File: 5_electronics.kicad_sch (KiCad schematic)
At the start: 10 parts, among them J1 Conn_02x20_Odd_Even

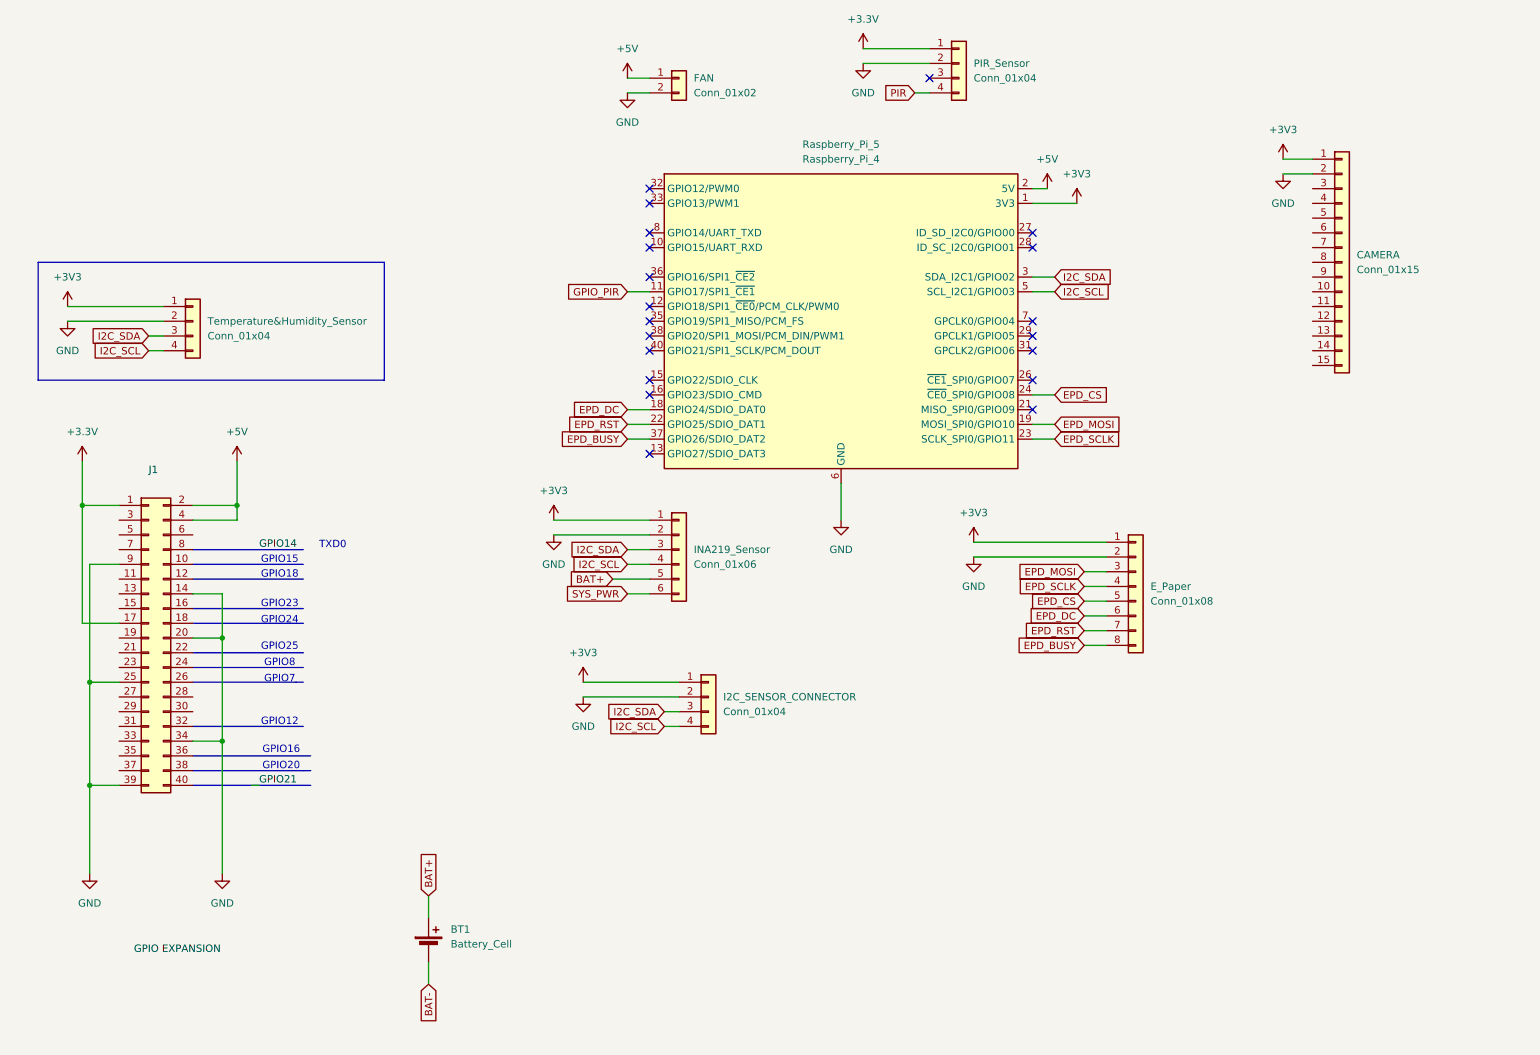
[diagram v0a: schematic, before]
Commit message: Update gpio pins
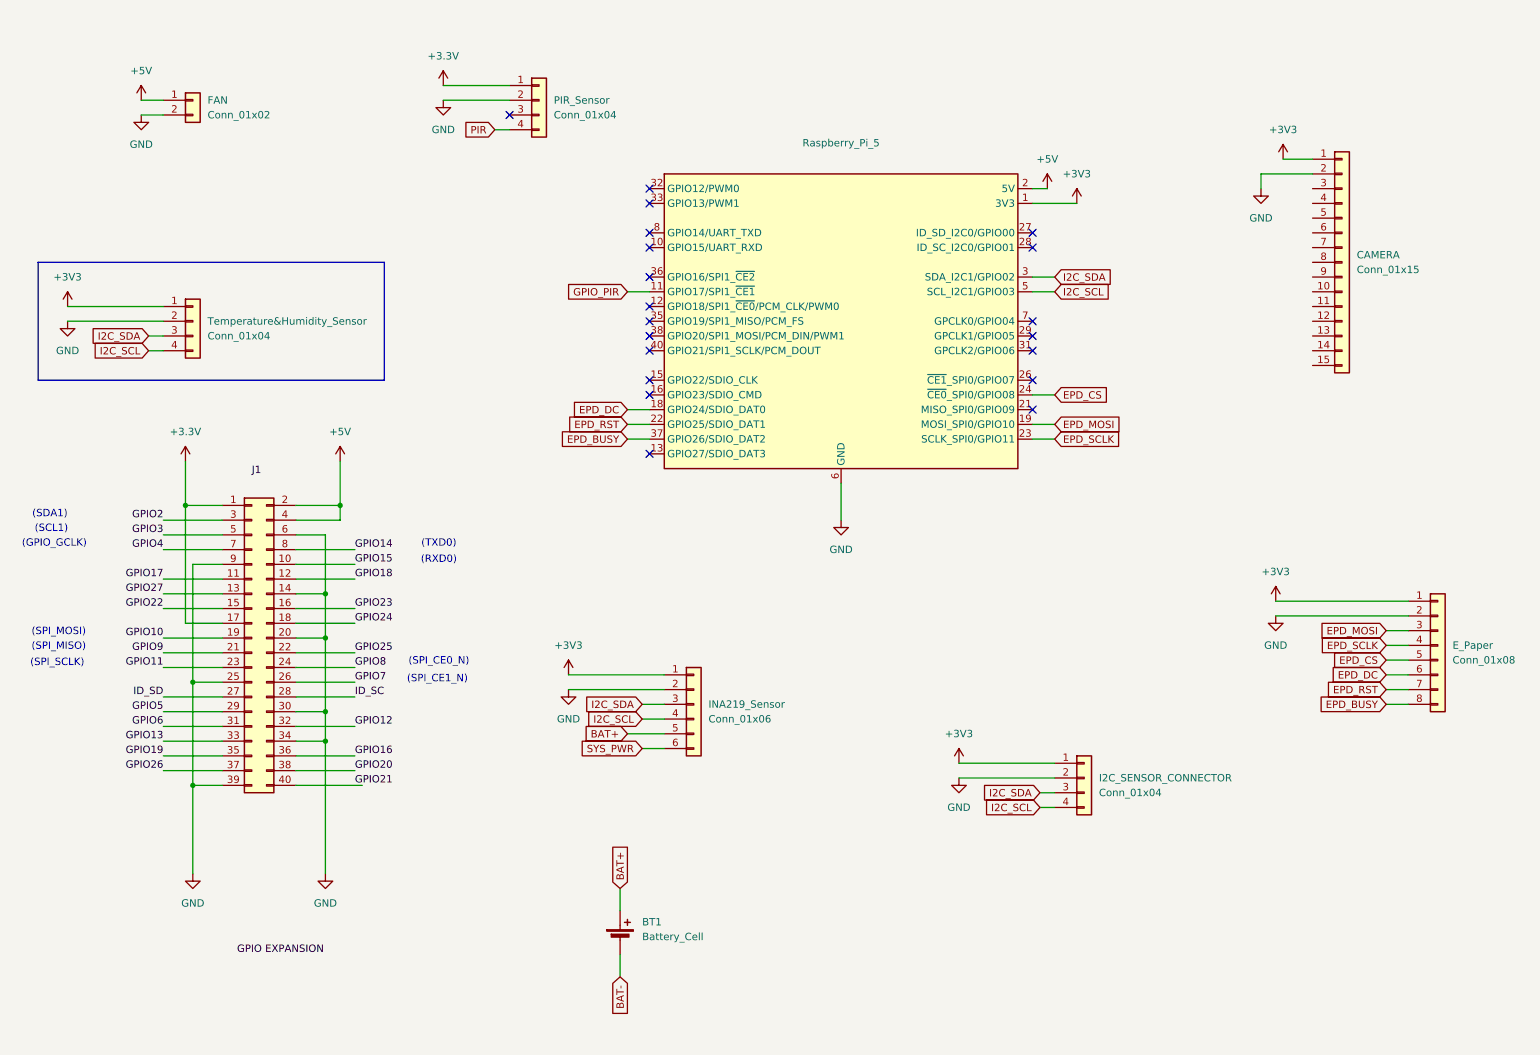
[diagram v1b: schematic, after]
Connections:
- net GND: now also J1.30 (Pin_30), J1.6 (Pin_6)
- net GPIO14: now also J1.8 (Pin_8)
- net GPIO15: now reaches J1.10 (Pin_10)
- net GPIO17: now reaches J1.11 (Pin_11)
- net GPIO18: now reaches J1.12 (Pin_12)
- net GPIO27: now reaches J1.13 (Pin_13)
- net GPIO22: now reaches J1.15 (Pin_15)
- net GPIO23: now reaches J1.16 (Pin_16)
- net GPIO24: now reaches J1.18 (Pin_18)
- net GPIO10: now reaches J1.19 (Pin_19)
- net GPIO9: now reaches J1.21 (Pin_21)
- net GPIO25: now reaches J1.22 (Pin_22)
- net GPIO11: now reaches J1.23 (Pin_23)
- net GPIO8: now reaches J1.24 (Pin_24)
- net GPIO7: now reaches J1.26 (Pin_26)
- net ID_SD: now reaches J1.27 (Pin_27)
- net ID_SC: now reaches J1.28 (Pin_28)
- net GPIO5: now reaches J1.29 (Pin_29)
- net GPIO2: now reaches J1.3 (Pin_3)
- net GPIO6: now reaches J1.31 (Pin_31)
- net GPIO12: now reaches J1.32 (Pin_32)
- net GPIO13: now reaches J1.33 (Pin_33)
- net GPIO19: now reaches J1.35 (Pin_35)
- net GPIO16: now reaches J1.36 (Pin_36)
- net GPIO26: now reaches J1.37 (Pin_37)
- net GPIO20: now reaches J1.38 (Pin_38)
- net at J1.40 (Pin_40): no longer names the net of J1.40 (Pin_40)
- net GPIO3: now reaches J1.5 (Pin_5)
- net GPIO4: now reaches J1.7 (Pin_7)
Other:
- note added: "(GPIO_GCLK)"
- note added: "(RXD0)"
- note added: "(SCL1)"
- note added: "(SDA1)"
- note added: "(SPI_CE0_N)"
- note added: "(SPI_CE1_N)"
- note added: "(SPI_MISO)"
- note added: "(SPI_MOSI)"
- note added: "(SPI_SCLK)"
- note added: "(TXD0)"
- note removed: "GPIO12"
- note removed: "GPIO15"
- note removed: "GPIO16"
- note removed: "GPIO18"
- note removed: "GPIO20"
- note removed: "GPIO23"
- note removed: "GPIO24"
- note removed: "GPIO25"
- note removed: "GPIO7"
- note removed: "GPIO8"
- note removed: "TXD0"
- moved on the sheet: BT1, E_Paper, FAN, I2C_SENSOR_CONNECTOR, INA219_Sensor, PIR_Sensor

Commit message: Update page setting
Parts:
- BT1: footprint (none) -> Battery:BatteryHolder_Keystone_103_1x20mm
- CAMERA1: renamed from CAMERA; footprint (none) -> Connector_PinHeader_2.54mm:PinHeader_1x15_P2.54mm_Vertical
- E_Paper1: renamed from E_Paper; footprint (none) -> Connector_PinHeader_2.54mm:PinHeader_1x08_P2.54mm_Vertical
- FAN1: renamed from FAN; footprint (none) -> Connector_PinHeader_2.54mm:PinHeader_1x02_P2.54mm_Vertical
- I2C_SENSOR_CONNECTOR1: renamed from I2C_SENSOR_CONNECTOR; footprint (none) -> Connector_PinHeader_2.54mm:PinHeader_1x04_P2.54mm_Vertical
- INA219_Sensor1: renamed from INA219_Sensor; footprint (none) -> Connector_PinHeader_2.54mm:PinHeader_1x06_P2.54mm_Vertical
- PIR_Sensor1: renamed from PIR_Sensor; footprint (none) -> Connector_PinHeader_2.54mm:PinHeader_1x04_P2.54mm_Vertical
- Temperature&Humidity_Sensor1: renamed from Temperature&Humidity_Sensor; footprint (none) -> Connector_PinHeader_2.54mm:PinHeader_1x04_P2.54mm_Vertical
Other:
- title: Raspberry Pi 4 Module B -> Smart Camera System
- moved on the sheet: E_Paper1
